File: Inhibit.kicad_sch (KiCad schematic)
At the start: 13 parts, among them U901 74HC595, U902 74HC595

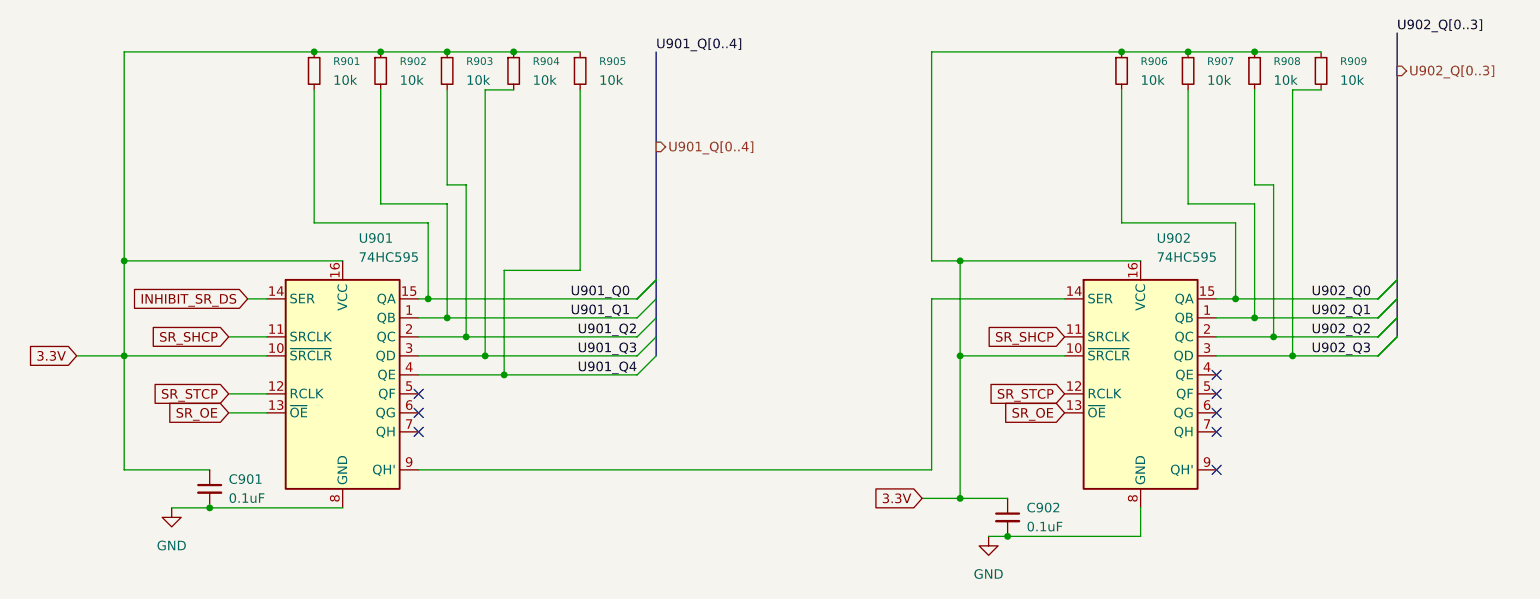
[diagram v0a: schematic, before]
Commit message: Removed un-needed inhibit from amp out. thereby simplifying the shift registers.
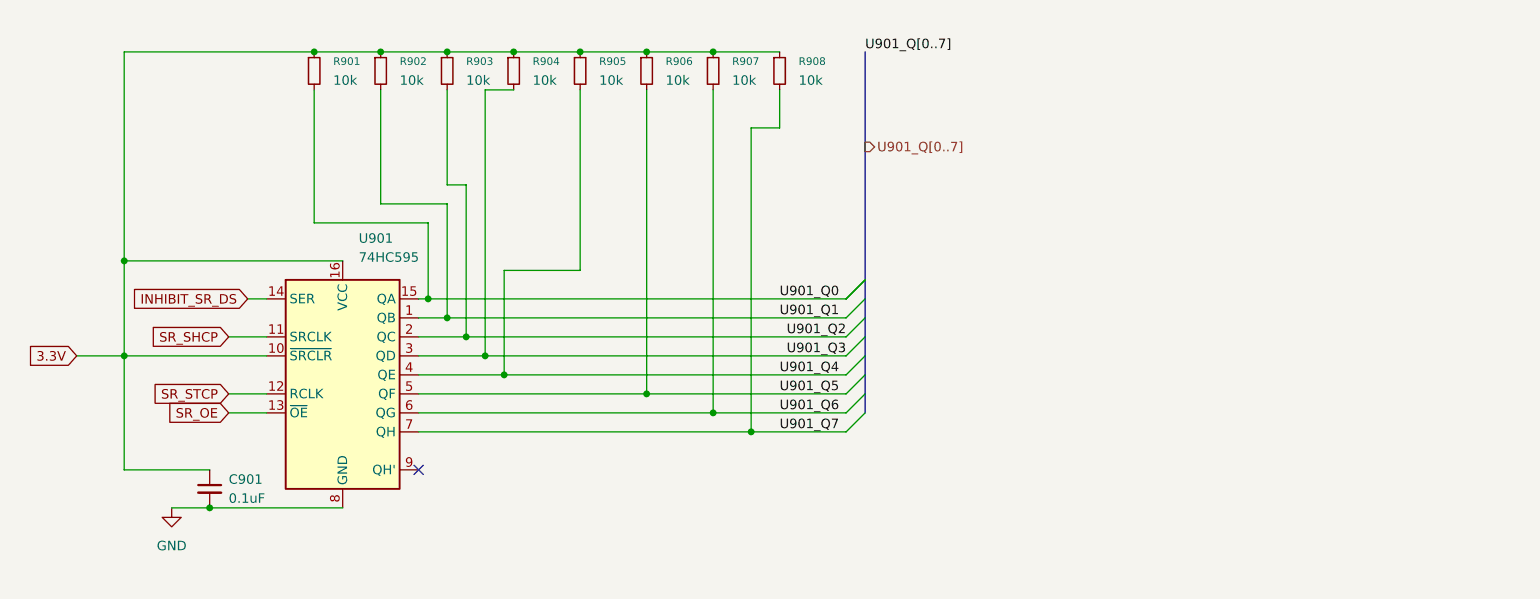
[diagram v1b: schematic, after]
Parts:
- removed C902: 0.1uF, Capacitor_THT:C_Disc_D5.0mm_W2.5mm_P2.50mm, symbol Device:C_Small
- removed R909: 10k, Resistor_THT:R_Axial_DIN0207_L6.3mm_D2.5mm_P7.62mm_Horizontal, symbol Device:R_Small
- removed U902: 74HC595, Package_DIP:DIP-16_W7.62mm, symbol 74xx:74HC595
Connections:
- net U902_Q0 is gone; now on net U901_Q5: R906.2
- net U902_Q1 is gone; now on net U901_Q6: R907.2
- net U902_Q2 is gone; now on net U901_Q7: R908.2
- net U901_Q5: now reaches U901.5 (QF)
- net U901_Q6: now reaches U901.6 (QG)
- net U901_Q7: now reaches U901.7 (QH)
- no-connect marks 8 -> 1
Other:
- moved on the sheet: R906, R907, R908
